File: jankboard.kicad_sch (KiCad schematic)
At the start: 21 parts, among them SW1 SW_Push_45deg, SW10 SW_Push_45deg, SW11 SW_Push_45deg, SW12 SW_Push_45deg, SW13 SW_Push_45deg, SW14 SW_Push_45deg, SW15 SW_Push_45deg, SW16 SW_Push_45deg, SW17 SW_Push_45deg, SW18 SW_Push_45deg, SW19 SW_Push_45deg, SW2 SW_Push_45deg, SW20 SW_Push_45deg, SW21 SW_Push_45deg, SW3 SW_Push_45deg, SW4 SW_Push_45deg, SW5 SW_Push_45deg, SW6 SW_Push_45deg, SW7 SW_Push_45deg, SW8 SW_Push_45deg, SW9 SW_Push_45deg

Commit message: gross shcematiasdf
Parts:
- added C1, C10, C11, C12, C13, C14, C15, C16, C17, C18, C19, C2, C20, C21, C22, C23, C24, C25, C26, C27, C28, C29, C3, C30, C31, C32, C33, C34, C4, C5, C6, C7, C8, C9: C, symbol Device:C
- added D1, D10, D11, D12, D13, D14, D15, D16, D17, D18, D19, D2, D20, D21, D22, D23, D24, D25, D26, D27, D28, D29, D3, D30, D31, D32, D33, D34, D35, D36, D37, D38, D39, D4, D40, D41, D42, D5, D6, D7, D8, D9: D, symbol Device:D
- added D43, D44, D45, D46, D47, D48, D49, D50, D51, D52, D53, D54, D55, D56, D57, D58, D59, D60, D61, D62, D63, D64, D65, D66, D67, D68, D69, D70, D71, D72, D73, D74, D75, D76, D77, D78, D79, D80, D81, D82, D83, D84: SK6812MINI, LED_SMD:LED_SK6812MINI_PLCC4_3.5x3.5mm_P1.75mm, symbol LED:SK6812MINI
- added D85, D86: MBR0530, Diode_SMD:D_SOD-123, symbol Diode:MBR0530
- added J1, J2: F31L-1A7H1-11030, F31L-1A7H1-11030:AMPHENOL_F31L-1A7H1-11030, symbol F31L-1A7H1-11030:F31L-1A7H1-11030
- added J3, J4: Conn_01x02, symbol Connector_Generic:Conn_01x02
- added R1, R2, R3, R4, R5, R6, R7, R8: R, symbol Device:R
- added U1: nice_nano, symbol nice_nano:nice_nano
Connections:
- net COL2: now reaches SW3.1
- net COL2: now also SW15.1, SW9.1, U1.5 (P0.17)
- net at SW3.2: now also D24.2 (A), D3.2 (A)
- net COL3: now reaches SW4.1
- net COL3: now also SW10.1, SW16.1, U1.6 (P0.20)
- net at SW4.2: now also D25.2 (A), D4.2 (A)
- net COL0: now reaches SW1.1
- net COL0: now also SW13.1, SW7.1, U1.1 (TX0/P0.06)
- net at SW1.2: now also D1.2 (A), D22.2 (A)
- net COL1: now reaches SW2.1
- net COL1: now also SW14.1, SW8.1, U1.2 (RX1/P0.08)
- net at SW2.2: now also D2.2 (A), D23.2 (A)
- net COL6: now reaches SW21.1
- net COL6: now also SW19.1, SW20.1, U1.9 (P1.00)
- net at SW21.2: now also D21.2 (A), D42.2 (A)
- net COL5: now reaches SW6.1
- net COL5: now also SW12.1, SW18.1, U1.8 (P0.24)
- net at SW6.2: now also D27.2 (A), D6.2 (A)
- net at SW12.2: now also D12.2 (A), D33.2 (A)
- net at SW20.2: now also D20.2 (A), D41.2 (A)
- net at SW10.2: now also D10.2 (A), D31.2 (A)
- net COL4: now reaches SW17.1
- net COL4: now also SW11.1, SW5.1, U1.7 (P0.22)
- net at SW17.2: now also D17.2 (A), D38.2 (A)
- net at SW15.2: now also D15.2 (A), D36.2 (A)
- net at SW19.2: now also D19.2 (A), D40.2 (A)
- net at SW14.2: now also D14.2 (A), D35.2 (A)
- net at SW11.2: now also D11.2 (A), D32.2 (A)
- net at SW16.2: now also D16.2 (A), D37.2 (A)
- net at SW18.2: now also D18.2 (A), D39.2 (A)
- net at SW7.2: now also D28.2 (A), D7.2 (A)
- net at SW9.2: now also D30.2 (A), D9.2 (A)
- net at SW8.2: now also D29.2 (A), D8.2 (A)
- net at SW5.2: now also D26.2 (A), D5.2 (A)
- net at SW13.2: now also D13.2 (A), D34.2 (A)
- new net: C26.2, J2.28
- new net: D70.1 (DOUT), D71.3 (DIN)
- new net: D69.1 (DOUT), D70.3 (DIN)
- new net: C23.2, J2.13
- new net: C9.2, D85.2 (A), J1.15
- new net: C22.2, J2.12
- new net: C15.2, J1.28
- new net: C18.2, C19.2, J2.11
- new net: C20.2, D86.2 (A), J2.15
- new net: D74.1 (DOUT), D75.3 (DIN)
- new net: D73.1 (DOUT), D74.3 (DIN)
- new net: D75.1 (DOUT), D76.3 (DIN)
- new net: D47.1 (DOUT), D48.3 (DIN)
- new net: D46.1 (DOUT), D47.3 (DIN)
- new net: D65.1 (DOUT), D66.3 (DIN)
- new net: D64.1 (DOUT), D65.3 (DIN)
- new net: D57.1 (DOUT), D58.3 (DIN)
- new net: D56.1 (DOUT), D57.3 (DIN)
- new net: D62.1 (DOUT), D63.3 (DIN)
- new net: D58.1 (DOUT), D59.3 (DIN)
- new net: C3.2, C4.2, J1.11
- new net: J1.8, R1.2
- new net: C27.2, J2.29
- new net: C29.1, J2.17
- new net: C29.2, J2.16
- new net: C10.1, J1.19
- new net: C10.2, J1.18
- new net: C28.2, J2.30
- new net: D71.1 (DOUT), D72.3 (DIN)
- new net: C6.2, J1.13
- new net: D60.1 (DOUT), D61.3 (DIN)
- new net: D59.1 (DOUT), D60.3 (DIN)
- new net: D68.1 (DOUT), D69.3 (DIN)
- new net: D83.1 (DOUT), D84.3 (DIN)
- new net: D82.1 (DOUT), D83.3 (DIN)
- new net: D61.1 (DOUT), D62.3 (DIN)
- new net: D43.1 (DOUT), D44.3 (DIN)
- new net: C34.1, J2.27
- new net: C34.2, J2.26
- new net: D76.1 (DOUT), D77.3 (DIN)
- new net: J3.1 (Pin_1), J4.1 (Pin_1), U1.24 (BATIN/P0.04)
- new net: D72.1 (DOUT), D73.3 (DIN)
- new net: J1.10, R2.1
- new net: D45.1 (DOUT), D46.3 (DIN)
- new net: D80.1 (DOUT), D81.3 (DIN)
- new net: D79.1 (DOUT), D80.3 (DIN)
- new net: D55.1 (DOUT), D56.3 (DIN)
- new net: D44.1 (DOUT), D45.3 (DIN)
- new net: D48.1 (DOUT), D49.3 (DIN)
- new net: C13.1, J1.25
- new net: C13.2, J1.24
- new net: D78.1 (DOUT), D79.3 (DIN)
- new net: D77.1 (DOUT), D78.3 (DIN)
- new net: J2.10, R4.1
- new net: C24.2, J2.14
- new net: C30.2, J2.18
- new net: C30.1, J2.19
- new net: C31.2, J2.20
- new net: C31.1, J2.21
- new net: C32.2, J2.22
- new net: C32.1, J2.23
- new net: C33.2, J2.24
- new net: C33.1, J2.25
- new net: J2.8, R3.2
- new net: D81.1 (DOUT), D82.3 (DIN)
- new net: D50.1 (DOUT), D51.3 (DIN)
- new net: D49.1 (DOUT), D50.3 (DIN)
- new net: D52.1 (DOUT), D53.3 (DIN)
- new net: D51.1 (DOUT), D52.3 (DIN)
- new net: C14.1, J1.27
- new net: C14.2, J1.26
- new net: C17.2, J1.30
- new net: D53.1 (DOUT), D54.3 (DIN)
- new net: C11.1, J1.21
- new net: C11.2, J1.20
- new net: D67.1 (DOUT), D68.3 (DIN)
- new net: D66.1 (DOUT), D67.3 (DIN)
- new net: D54.1 (DOUT), D55.3 (DIN)
- new net: C7.2, J1.14
- new net: C16.2, J1.29
- new net: C8.1, J1.17
- new net: C8.2, J1.16
- new net: C5.2, J1.12
- new net: C12.2, J1.22
- new net: C12.1, J1.23
- new net +3.3V: C1.1, C2.1, C21.1, C25.1, D43.4 (VDD), D44.4 (VDD), D45.4 (VDD), D46.4 (VDD), D47.4 (VDD), D48.4 (VDD), D49.4 (VDD), D50.4 (VDD), D51.4 (VDD), D52.4 (VDD), D53.4 (VDD), D54.4 (VDD), D55.4 (VDD), D56.4 (VDD), D57.4 (VDD), D58.4 (VDD), D59.4 (VDD), D60.4 (VDD), D61.4 (VDD), D62.4 (VDD), D63.4 (VDD), D64.4 (VDD), D65.4 (VDD), D66.4 (VDD), D67.4 (VDD), D68.4 (VDD), D69.4 (VDD), D70.4 (VDD), D71.4 (VDD), D72.4 (VDD), D73.4 (VDD), D74.4 (VDD), D75.4 (VDD), D76.4 (VDD), D77.4 (VDD), D78.4 (VDD), D79.4 (VDD), D80.4 (VDD), D81.4 (VDD), D82.4 (VDD), D83.4 (VDD), D84.4 (VDD), J1.3, J2.3, R1.1, R3.1, R5.1, R6.1, R7.1, R8.1, U1.21 (VCC)
- new net BUSY: J1.9, J2.9, U1.20 (AIN7/P0.31)
- new net CS: J1.6, J2.6, U1.18 (AIN0/P0.02)
- new net DC: J1.7, J2.7, U1.19 (AIN5/P0.29)
- new net DIN: J1.4, J2.4, U1.16 (P1.13)
- new net GND: C1.2, C15.1, C16.1, C17.1, C18.1, C19.1, C2.2, C20.1, C21.2, C22.1, C23.1, C24.1, C25.2, C26.1, C27.1, C28.1, C3.1, C4.1, C5.1, C6.1, C7.1, C9.1, D43.2 (VSS), D44.2 (VSS), D45.2 (VSS), D46.2 (VSS), D47.2 (VSS), D48.2 (VSS), D49.2 (VSS), D50.2 (VSS), D51.2 (VSS), D52.2 (VSS), D53.2 (VSS), D54.2 (VSS), D55.2 (VSS), D56.2 (VSS), D57.2 (VSS), D58.2 (VSS), D59.2 (VSS), D60.2 (VSS), D61.2 (VSS), D62.2 (VSS), D63.2 (VSS), D64.2 (VSS), D65.2 (VSS), D66.2 (VSS), D67.2 (VSS), D68.2 (VSS), D69.2 (VSS), D70.2 (VSS), D71.2 (VSS), D72.2 (VSS), D73.2 (VSS), D74.2 (VSS), D75.2 (VSS), D76.2 (VSS), D77.2 (VSS), D78.2 (VSS), D79.2 (VSS), D80.2 (VSS), D81.2 (VSS), D82.2 (VSS), D83.2 (VSS), D84.2 (VSS), D85.1 (K), D86.1 (K), J1.2, J2.2, J3.2 (Pin_2), J4.2 (Pin_2), R2.2, R4.2, U1.23 (GND), U1.3 (GND), U1.4 (GND)
- new net NEO: D43.3 (DIN), D64.3 (DIN), U1.13 (NFC1/P0.09)
- new net ROW0: D1.1 (K), D19.1 (K), D2.1 (K), D22.1 (K), D23.1 (K), D24.1 (K), D25.1 (K), D26.1 (K), D27.1 (K), D3.1 (K), D4.1 (K), D40.1 (K), D5.1 (K), D6.1 (K), U1.10 (P0.11)
- new net ROW1: D10.1 (K), D11.1 (K), D12.1 (K), D20.1 (K), D28.1 (K), D29.1 (K), D30.1 (K), D31.1 (K), D32.1 (K), D33.1 (K), D41.1 (K), D7.1 (K), D8.1 (K), D9.1 (K), U1.11 (P1.04)
- new net ROW2: D13.1 (K), D14.1 (K), D15.1 (K), D16.1 (K), D17.1 (K), D18.1 (K), D21.1 (K), D34.1 (K), D35.1 (K), D36.1 (K), D37.1 (K), D38.1 (K), D39.1 (K), D42.1 (K), U1.12 (P1.06)
- new net SCK: J1.5, J2.5, U1.17 (P1.15)
- new net SCL: R6.2, R8.2, U1.15 (P1.11)
- new net SDA: R5.2, R7.2, U1.14 (NFC2/P0.10)
- no-connect marks 0 -> 8
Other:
- moved on the sheet: SW1, SW10, SW11, SW12, SW13, SW14, SW15, SW16, SW17, SW18, SW19, SW2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

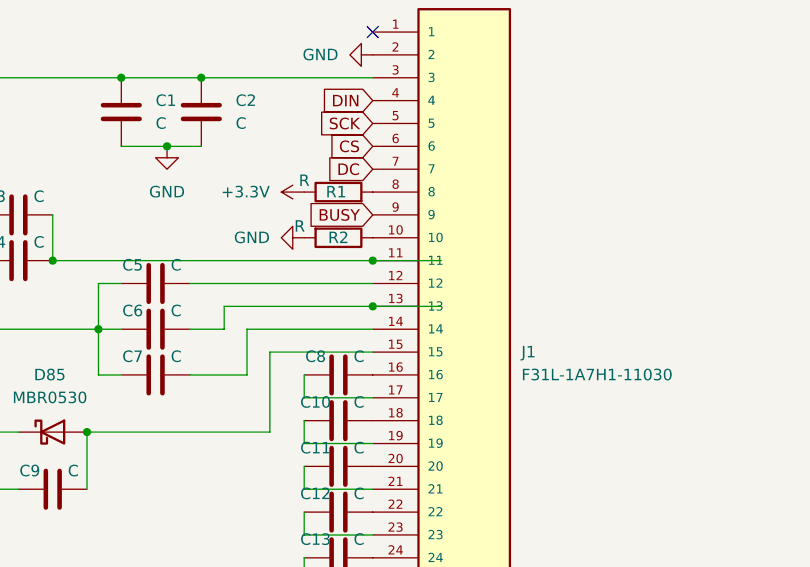
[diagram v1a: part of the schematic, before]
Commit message: add low profile switch library
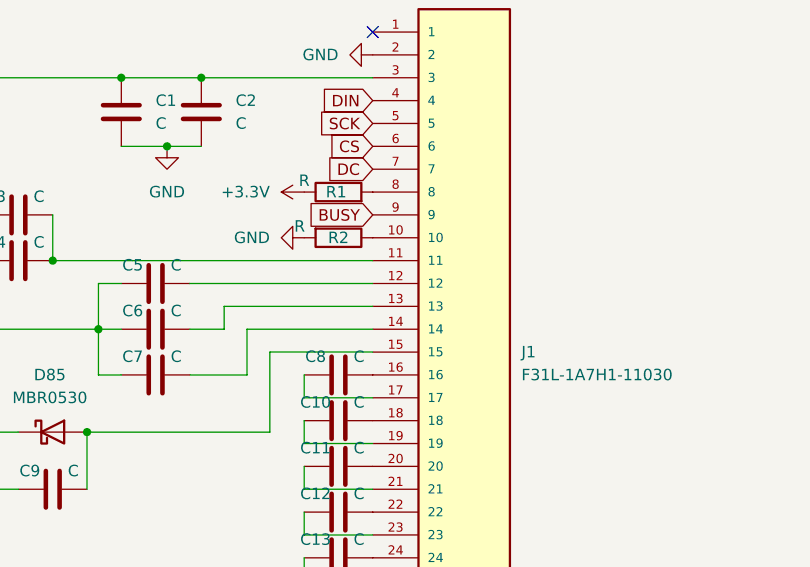
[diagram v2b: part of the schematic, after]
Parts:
- C1, C10, C11, C12, C13, C14, C15, C16, C17, C18, C19, C2, C20, C21, C22, C23, C24, C25, C26, C27, C28, C29, C3, C30, C31, C32, C33, C34, C4, C5, C6, C7, C8, C9: footprint (none) -> Capacitor_SMD:C_1206_3216Metric
- D1, D10, D11, D12, D13, D14, D15, D16, D17, D18, D19, D2, D20, D21, D22, D23, D24, D25, D26, D27, D28, D29, D3, D30, D31, D32, D33, D34, D35, D36, D37, D38, D39, D4, D40, D41, D42, D5, D6, D7, D8, D9: footprint (none) -> Diode_SMD:D_1206_3216Metric
- R1, R2, R3, R4, R5, R6, R7, R8: footprint (none) -> Resistor_SMD:R_1206_3216Metric
- U1: footprint (none) -> nice-nano-kicad:nice_nano

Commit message: place keys and leds
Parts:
- C1, C10, C11, C12, C13, C14, C15, C16, C17, C18, C19, C2, C20, C21, C22, C23, C24, C25, C26, C27, C28, C29, C3, C30, C31, C32, C33, C34, C4, C5, C6, C7, C8, C9: footprint Capacitor_SMD:C_1206_3216Metric -> Capacitor_SMD:C_0603_1608Metric
- J1, J2: footprint F31L-1A7H1-11030:AMPHENOL_F31L-1A7H1-11030 -> connector:F31L-1A7H1-11030
- J3, J4: footprint (none) -> Connector_JST:JST_EH_S2B-EH_1x02_P2.50mm_Horizontal
- R1, R2, R3, R4, R5, R6, R7, R8: footprint Resistor_SMD:R_1206_3216Metric -> Resistor_SMD:R_0612_1632Metric
- SW1, SW10, SW11, SW12, SW13, SW14, SW15, SW16, SW17, SW18, SW19, SW2, SW20, SW21, SW3, SW4, SW5, SW6, SW7, SW8, SW9: footprint (none) -> keyswitches:SW_PG1350_reversible

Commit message: connectors
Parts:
- added J5: Conn_01x04_Pin, symbol Connector:Conn_01x04_Pin
- added SW22, SW23: SW_SPDT, symbol Switch:SW_SPDT
- J3, J4: footprint Connector_JST:JST_EH_S2B-EH_1x02_P2.50mm_Horizontal -> Connector_JST:JST_PH_S2B-PH-SM4-TB_1x02-1MP_P2.00mm_Horizontal
- R1, R2, R3, R4, R5, R6, R7, R8: footprint Resistor_SMD:R_0612_1632Metric -> Resistor_SMD:R_0603_1608Metric
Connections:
- net +3.3V: now also C18.1, C19.1, J5.1 (Pin_1); no longer C21.1, C25.1
- net BUSY: now also U1.19 (AIN5/P0.29); no longer U1.20 (AIN7/P0.31)
- net CS: now also U1.17 (P1.15); no longer U1.18 (AIN0/P0.02)
- net DC: now also U1.18 (AIN0/P0.02); no longer U1.19 (AIN5/P0.29)
- net DIN: now also U1.15 (P1.11); no longer U1.16 (P1.13)
- net GND: now also C18.2, C19.2, C21.1, C32.1, C33.1, C34.1, J5.2 (Pin_2), SW22.2 (B), SW23.2 (B); no longer C18.1, C19.1, C21.2, C25.2, C27.1, C28.1, J3.2 (Pin_2), J4.2 (Pin_2)
- net NEO: now also U1.20 (AIN7/P0.31); no longer U1.13 (NFC1/P0.09)
- net SCK: now also U1.16 (P1.13); no longer U1.17 (P1.15)
- net SCL: now also U1.14 (NFC2/P0.10), J5.4 (Pin_4); no longer U1.15 (P1.11)
- net SDA: now also U1.13 (NFC1/P0.09), J5.3 (Pin_3); no longer U1.14 (NFC2/P0.10)
- net at C26.2: now also D86.2 (A), J2.15; no longer J2.28
- net at C27.2: now also J2.18; no longer J2.29
- net at C29.1: now also J2.23; no longer J2.17
- net at C29.2: now also J2.22; no longer J2.16
- net at C28.2: now also J2.20; no longer J2.30
- net at J2.27: now also C31.1; no longer C34.1
- net at C34.2: now also J2.30; no longer J2.26
- net at C30.2: now also J2.24; no longer J2.18
- net at J2.19: now also C27.1; no longer C30.1
- net at C31.2: now also J2.26; no longer J2.20
- net at J2.21: now also C28.1; no longer C31.1
- net at C32.2: now also J2.28; no longer J2.22
- net at C33.2: now also J2.29; no longer J2.24
- net at J2.25: now also C30.1; no longer C33.1
- new net: C20.2, C21.2, J2.11
- new net: J3.2 (Pin_2), J4.2 (Pin_2), SW22.1 (A), SW23.1 (A)
- new net: C25.2, J2.16
- new net: C25.1, J2.17
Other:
- moved on the sheet: C18, C19, C20, C21, C25, C26, C27, C28, C29, C30, C31, C32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

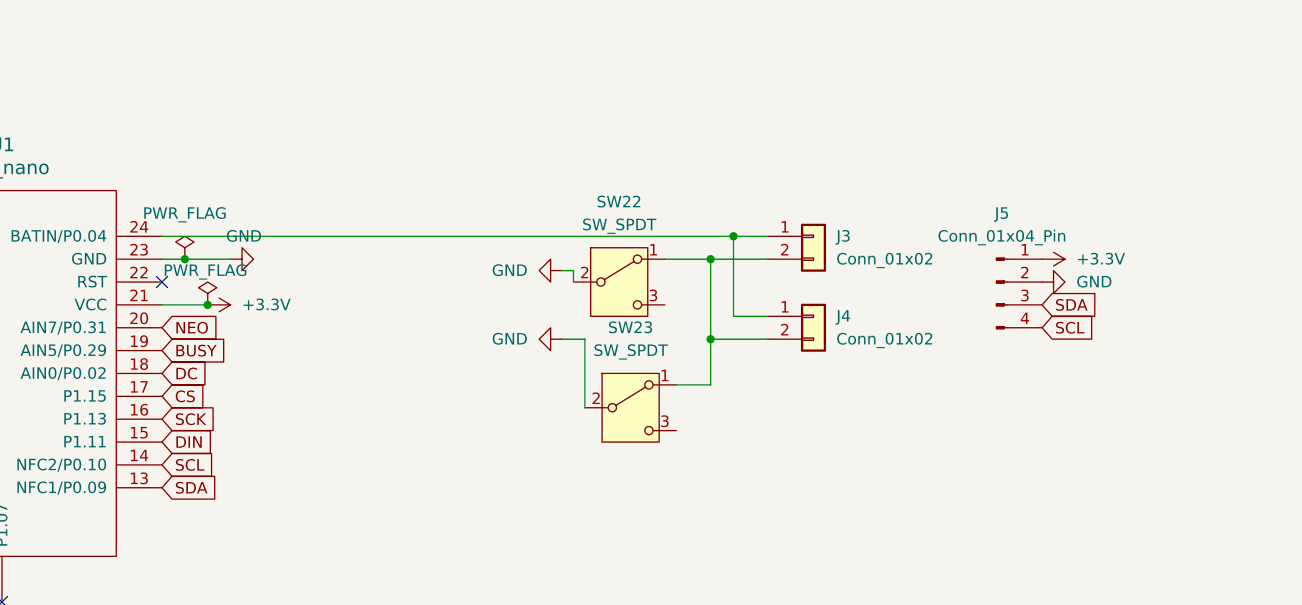
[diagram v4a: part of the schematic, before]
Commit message: design rule checking
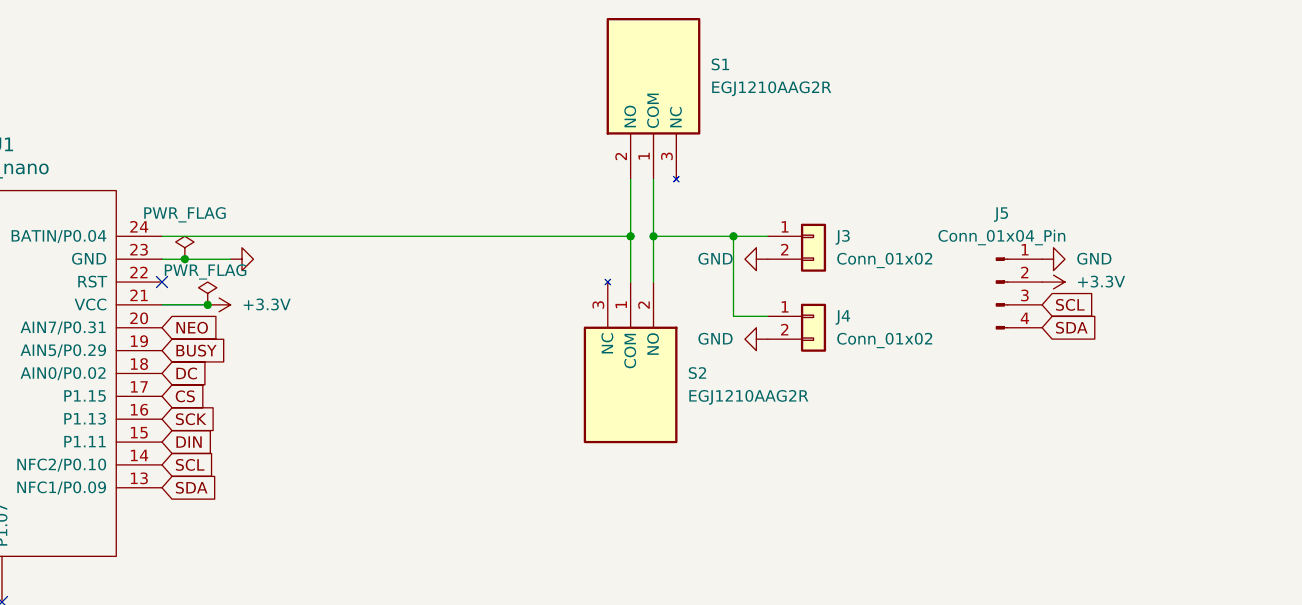
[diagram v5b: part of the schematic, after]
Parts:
- removed SW22, SW23: SW_SPDT, symbol Switch:SW_SPDT
- added S1, S2: EGJ1210AAG2R, KiCad:EGJ1210AAG2R, symbol EGJ1210AAG2R:EGJ1210AAG2R
- J5: footprint (none) -> Connector_PinHeader_1.00mm:PinHeader_1x04_P1.00mm_Vertical
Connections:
- net +3.3V: now also J5.2 (Pin_2); no longer J5.1 (Pin_1)
- net GND: now also J3.2 (Pin_2), J4.2 (Pin_2), J5.1 (Pin_1); no longer J5.2 (Pin_2)
- net SCL: now also J5.3 (Pin_3); no longer J5.4 (Pin_4)
- net SDA: now also J5.4 (Pin_4); no longer J5.3 (Pin_3)
- net at J3.1 (Pin_1), J4.1 (Pin_1): now also S1.1 (COM), S2.2 (NO); no longer U1.24 (BATIN/P0.04)
- new net: S1.2 (NO), S2.1 (COM), U1.24 (BATIN/P0.04)

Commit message: remove via on pins, change pin footprint
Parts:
- J5: footprint Connector_PinHeader_1.00mm:PinHeader_1x04_P1.00mm_Vertical -> Connector_PinHeader_2.54mm:PinHeader_1x04_P2.54mm_Vertical
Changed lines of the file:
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@@
 			)
 		)
-		(property "Footprint" "Connector_PinHeader_1.00mm:PinHeader_1x04_P1.00mm_Vertical"
+		(property "Footprint" "Connector_PinHeader_2.54mm:PinHeader_1x04_P2.54mm_Vertical"
 			(at 356.87 27.94 0)
 			(effects

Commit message: add led switch
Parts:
- added S3, S4: EGJ1210AAG2R, KiCad:EGJ1210AAG2R, symbol EGJ1210AAG2R:EGJ1210AAG2R
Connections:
- net +3.3V: now also S3.1 (COM), S4.2 (NO); no longer D43.4 (VDD), D44.4 (VDD), D45.4 (VDD), D46.4 (VDD), D47.4 (VDD), D48.4 (VDD), D49.4 (VDD), D50.4 (VDD), D51.4 (VDD), D52.4 (VDD), D53.4 (VDD), D54.4 (VDD), D55.4 (VDD), D56.4 (VDD), D57.4 (VDD), D58.4 (VDD), D59.4 (VDD), D60.4 (VDD), D61.4 (VDD), D62.4 (VDD), D63.4 (VDD), D64.4 (VDD), D65.4 (VDD), D66.4 (VDD), D67.4 (VDD), D68.4 (VDD), D69.4 (VDD), D70.4 (VDD), D71.4 (VDD), D72.4 (VDD), D73.4 (VDD), D74.4 (VDD), D75.4 (VDD), D76.4 (VDD), D77.4 (VDD), D78.4 (VDD), D79.4 (VDD), D80.4 (VDD), D81.4 (VDD), D82.4 (VDD), D83.4 (VDD), D84.4 (VDD)
- new net NP: D43.4 (VDD), D44.4 (VDD), D45.4 (VDD), D46.4 (VDD), D47.4 (VDD), D48.4 (VDD), D49.4 (VDD), D50.4 (VDD), D51.4 (VDD), D52.4 (VDD), D53.4 (VDD), D54.4 (VDD), D55.4 (VDD), D56.4 (VDD), D57.4 (VDD), D58.4 (VDD), D59.4 (VDD), D60.4 (VDD), D61.4 (VDD), D62.4 (VDD), D63.4 (VDD), D64.4 (VDD), D65.4 (VDD), D66.4 (VDD), D67.4 (VDD), D68.4 (VDD), D69.4 (VDD), D70.4 (VDD), D71.4 (VDD), D72.4 (VDD), D73.4 (VDD), D74.4 (VDD), D75.4 (VDD), D76.4 (VDD), D77.4 (VDD), D78.4 (VDD), D79.4 (VDD), D80.4 (VDD), D81.4 (VDD), D82.4 (VDD), D83.4 (VDD), D84.4 (VDD), S3.2 (NO), S4.1 (COM)
